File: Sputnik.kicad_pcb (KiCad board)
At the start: 4 copper layers, 130 x 60 mm, 78 parts, among them IC1 EP4CE10F17, J1 Pinheader_2x5_TH_WALL, U1 SN74LVC2T45, U10 SN74LVC8T245, U11 SN74LVC8T245, U12 SN74LVC8T245, U13 SN74LVC8T245, U14 SN74LVC8T245, U15 SN74LVC8T245, U16 SN74LVC2T45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

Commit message: Up
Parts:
- C16, U4: moved to B.Cu
- moved C16 51.4 mm to (231.4, 61.5), turned to 180 degrees
- moved U4 14.8 mm to (210.0, 61.5)
- moved U3 1.03 mm to (231.2, 61.5), turned to 270 degrees
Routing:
- net /Zorro/~SLAVEn: track 10.6 -> 15.7 mm
- net GND: track 126.6 -> 129.1 mm, vias 41 -> 43
- net +3V3: track 30.7 -> 33.1 mm, vias 7 -> 9

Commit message: More routing
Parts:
- C14, C34: moved to B.Cu
- moved C34 70.7 mm to (197.2, 65.0), turned to 180 degrees
- moved R8 1.50 mm to (197.2, 63.5)
- moved C14 1.30 mm to (197.2, 58.0), turned to 180 degrees
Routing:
- net /FPGA/TDO: track 0.71 -> 59.9 mm
- net /FPGA/TCK: track 0.71 -> 52.6 mm
- net /Zorro/~BRn: track 0.00 -> 47.3 mm, vias 0 -> 1
- net /Zorro/~CFGOUTn: track 0.00 -> 34.5 mm, vias 0 -> 2
- net /Zorro/~MTACK: track 0.00 -> 30.3 mm
- net /Zorro/~CINH: track 0.00 -> 25.8 mm, vias 0 -> 1
- net GND: track 129.1 -> 136.7 mm, vias 43 -> 50
- net Net-(R8-Pad1): track 0.00 -> 4.45 mm
- net +3V3: track 33.1 -> 34.6 mm, vias 9 -> 10
- net +5VDC: track 23.5 -> 24.9 mm, vias 8 -> 9

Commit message: And more
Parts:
- moved C42 2.83 mm to (152.7, 64.3), turned to 90 degrees
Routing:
- net Net-(R8-Pad1): track 4.45 -> 65.5 mm
- net /Zorro/~DTACK: track 0.00 -> 18.7 mm
- net GND: track 136.7 -> 153.9 mm, vias 50 -> 64
- net /Zorro/E_CLOCK: track 4.72 -> 20.6 mm, vias 1 -> 2
- net /Zorro/~INT6: track 0.00 -> 15.5 mm
- net /Zorro/~INT2: track 0.00 -> 13.7 mm, vias 0 -> 1
- net /Zorro/AD12: track 3.30 -> 12.5 mm
- net /Zorro/~CINH: track 25.8 -> 32.0 mm
- net +5VDC: track 24.9 -> 28.3 mm, vias 9 -> 13
- net +3V3: track 34.6 -> 36.3 mm, vias 10 -> 13
- net /Zorro/AD29: track 11.1 -> 11.8 mm
- net /Zorro/~DS0: track 24.9 -> 25.5 mm

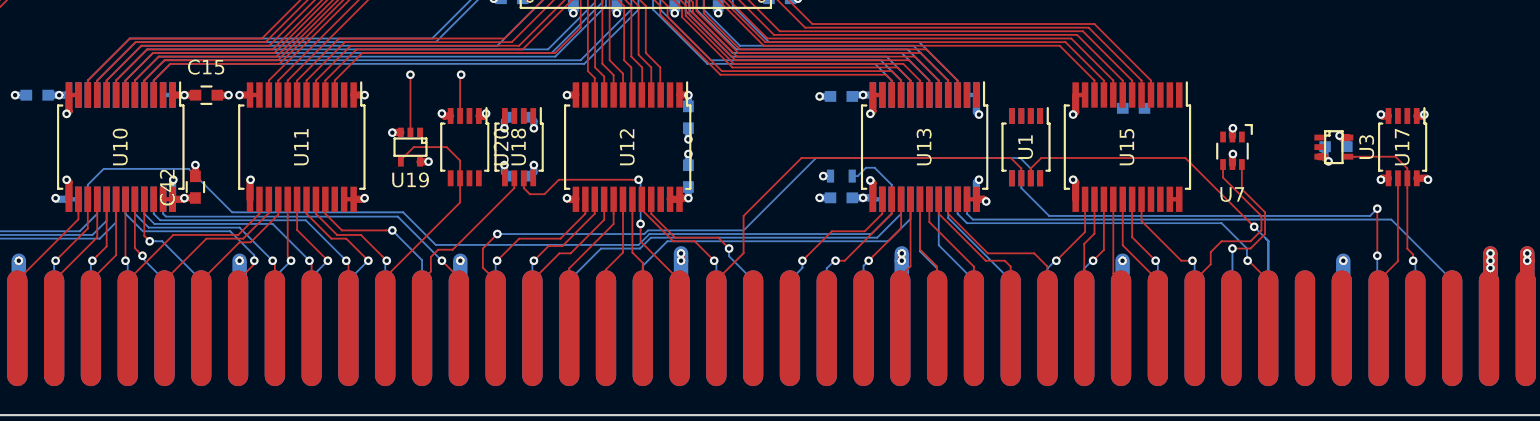
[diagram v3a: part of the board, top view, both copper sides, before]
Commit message: More routing and caps
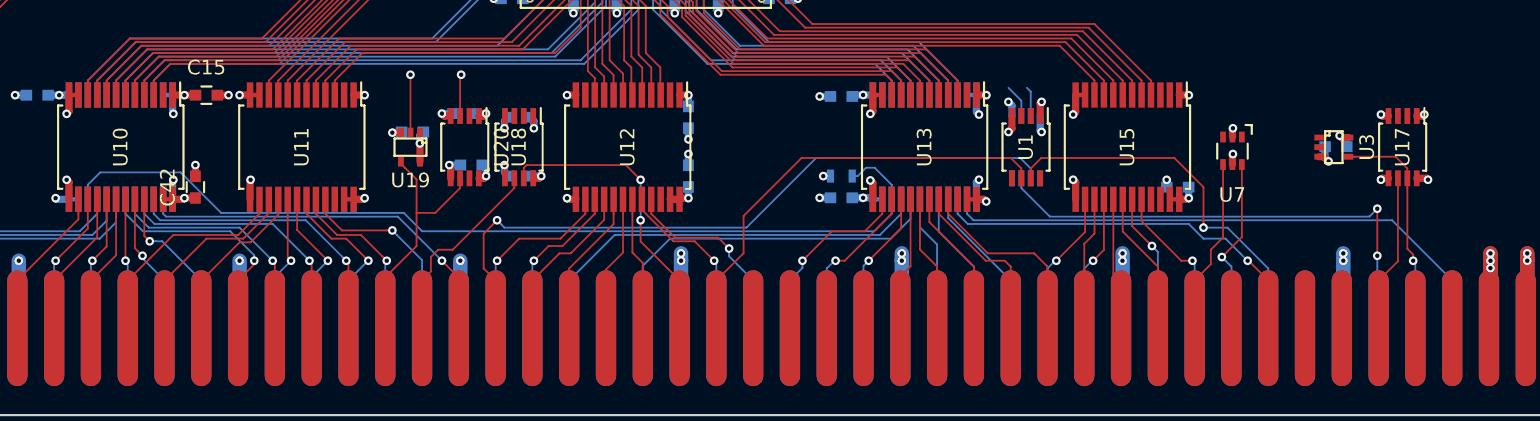
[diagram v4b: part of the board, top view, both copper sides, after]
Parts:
- added C61: 0,1, Capacitors_SMD:C_0603, B.Cu at (171.7, 62.7)
- added C62: 0,1, Capacitors_SMD:C_0603, B.Cu at (171.2, 59.2)
- added C63: 0,1, Capacitors_SMD:C_0603, B.Cu at (167.6, 60.5)
- moved C43 6.23 mm to (220.5, 64.3), turned to 180 degrees
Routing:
- net GND: track 153.9 -> 162.2 mm, vias 64 -> 71
- net +3V3: track 36.3 -> 42.1 mm, vias 13 -> 17
- net /Zorro/~CINH: track 32.0 -> 26.3 mm
- net /Zorro/~INT6: track 15.5 -> 12.1 mm
- net +5VDC: track 28.3 -> 30.8 mm, vias 13 -> 14
- net /FPGA/nCFGOUTn: track 0.00 -> 2.31 mm
- net /FPGA/nBR: track 0.00 -> 2.06 mm
- net /Zorro/~INT2: track 13.7 -> 12.1 mm
- net /Zorro/~DTACK: track 18.7 -> 17.3 mm
- net Net-(R8-Pad1): track 65.5 -> 64.5 mm
- net /Zorro/~BRn: track 47.3 -> 48.2 mm
- net (no net): vias 0 -> 1

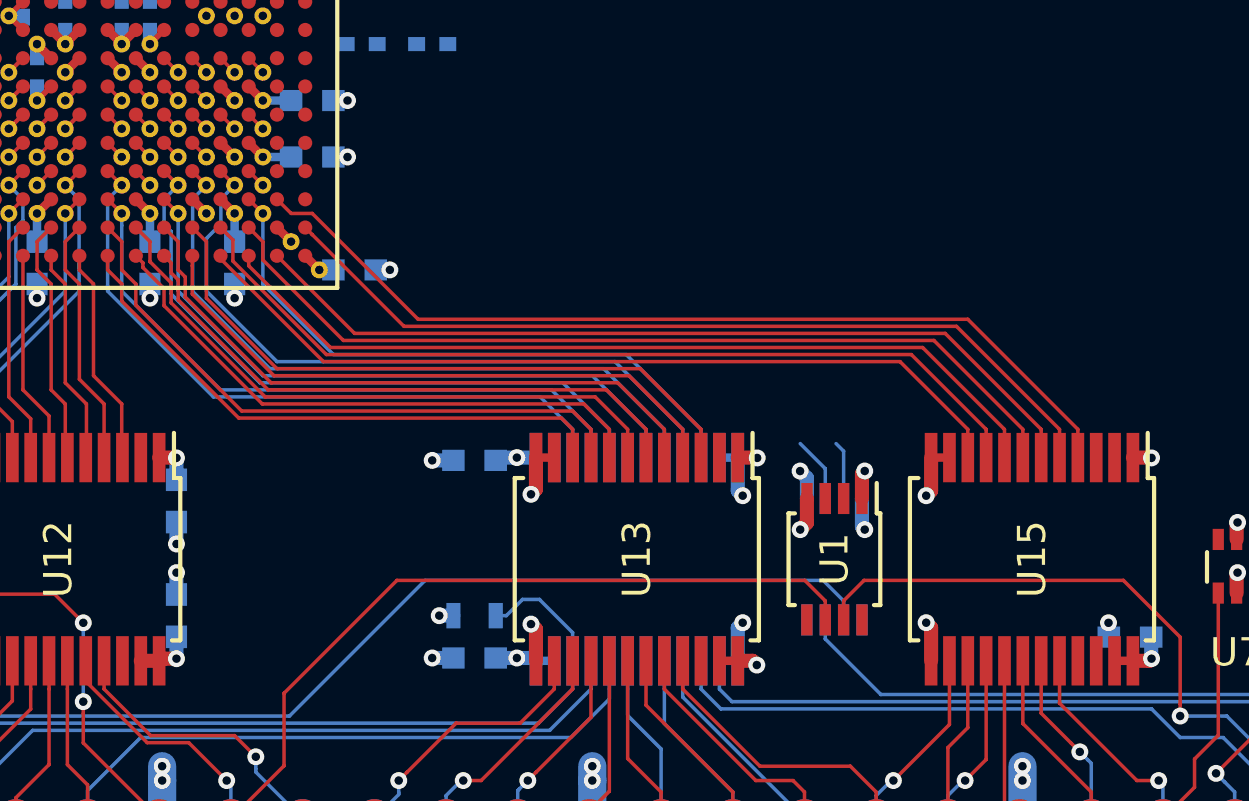
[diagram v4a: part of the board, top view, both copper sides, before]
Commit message: Added nMTACK and nCINH signals
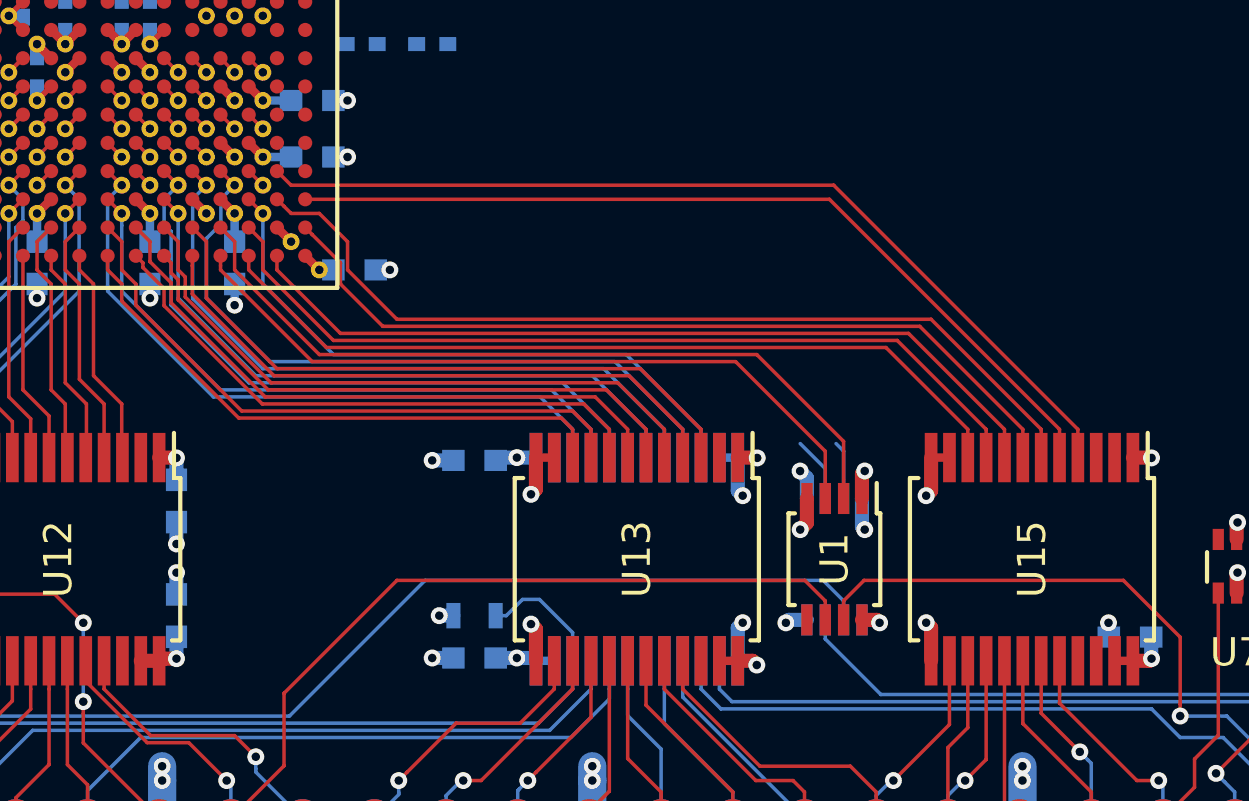
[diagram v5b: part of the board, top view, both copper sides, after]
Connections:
- IC1 pad N15: Net-(IC1-PadN15) -> /FPGA/A_5
- IC1 pad P15: /FPGA/A_5 -> /FPGA/A_4
- IC1 pad P16: Net-(IC1-PadP16) -> /FPGA/A_6
- IC1 pad R13: /FPGA/A_7 -> /FPGA/nCINH
- IC1 pad R14: /FPGA/A_3 -> /FPGA/A_7
- IC1 pad R16: /FPGA/A_6 -> /FPGA/A_3
- IC1 pad T13: /FPGA/nLOCK -> /FPGA/nMTACK
- IC1 pad T14: /FPGA/A_2 -> /FPGA/nLOCK
- IC1 pad T15: /FPGA/A_4 -> /FPGA/A_2
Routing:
- net /FPGA/nCINH: track 0.00 -> 27.8 mm
- net /FPGA/nMTACK: track 0.00 -> 26.4 mm
- net /FPGA/A_3: track 31.8 -> 29.8 mm
- net +5VDC: track 30.8 -> 32.2 mm, vias 14 -> 16
- net /FPGA/A_4: track 30.6 -> 32.0 mm
- net /FPGA/A_2: track 30.5 -> 29.6 mm
- net /FPGA/A_7: track 31.5 -> 30.7 mm
- net /FPGA/nLOCK: track 30.1 -> 29.3 mm

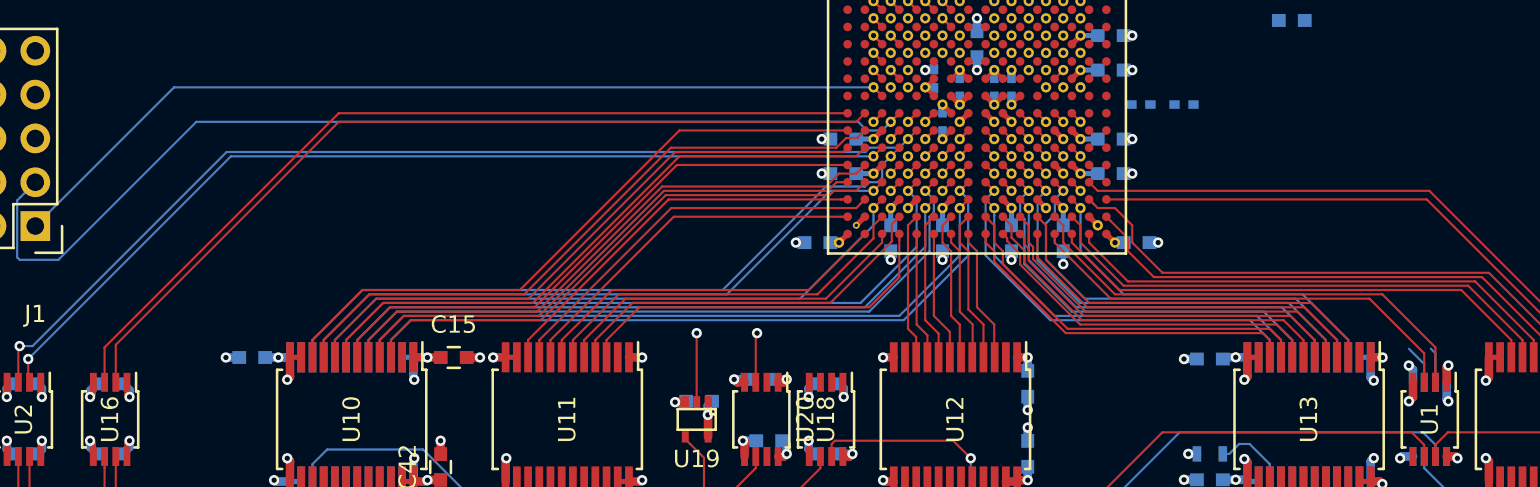
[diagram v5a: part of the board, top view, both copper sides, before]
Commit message: Squeezed nBG and E_CLOCK as well
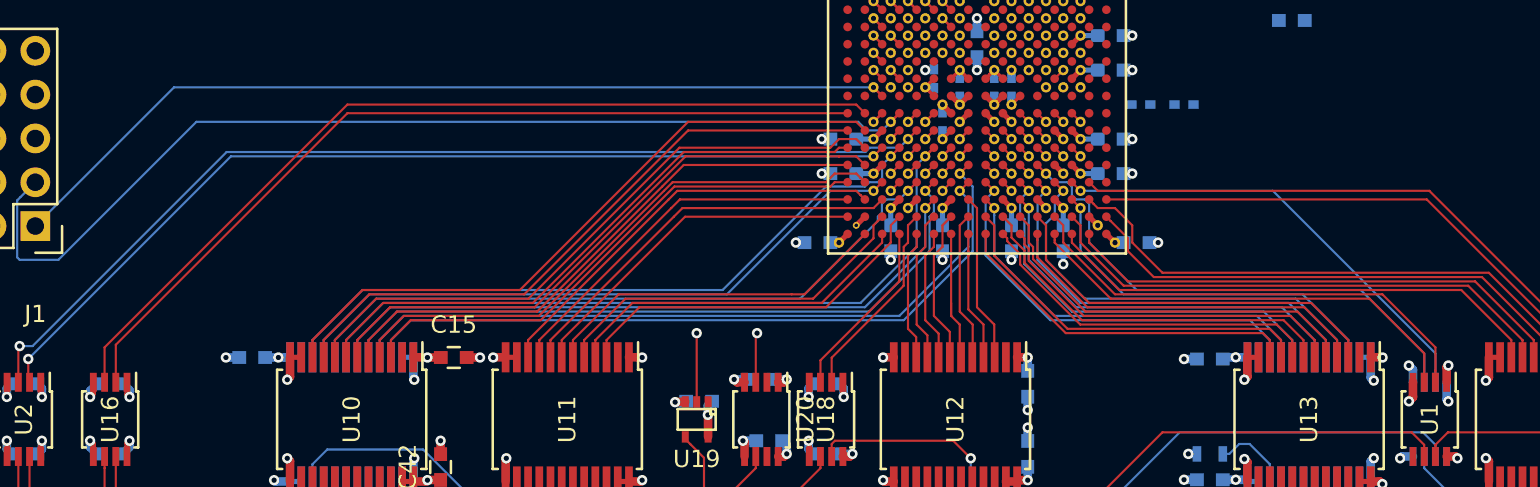
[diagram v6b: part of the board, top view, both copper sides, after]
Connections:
- IC1 pad J1: /FPGA/7M_ -> /FPGA/SenseZ3
- IC1 pad J2: /FPGA/SenseZ3 -> /FPGA/7M_
- IC1 pad K1: /FPGA/SD_5 -> /FPGA/SD_4
- IC1 pad K2: /FPGA/SD_4 -> /FPGA/SD_5
- IC1 pad L1: /FPGA/SD_6 -> /FPGA/SD_3
- IC1 pad L2: /FPGA/SD_3 -> /FPGA/SD_6
- IC1 pad L6: Net-(IC1-PadL6) -> /FPGA/nCCS
- IC1 pad M1: /FPGA/SD_7 -> /FPGA/SD_2
- IC1 pad M12: Net-(IC1-PadM12) -> /FPGA/nCFGOUTn
- IC1 pad M2: /FPGA/SD_2 -> /FPGA/SD_7
- IC1 pad M8: Net-(IC1-PadM8) -> /FPGA/nBGACK
- IC1 pad N1: /FPGA/SD_1 -> /FPGA/SD_0
- IC1 pad N14: Net-(IC1-PadN14) -> /FPGA/nBR
- IC1 pad N2: /FPGA/SD_0 -> /FPGA/SD_1
- IC1 pad N5: /FPGA/nCCS -> /FPGA/DOE_
- IC1 pad N8: /FPGA/nBGACK -> /FPGA/READ_
- IC1 pad P1: /FPGA/AD_24 -> /FPGA/AD_25
- IC1 pad P2: /FPGA/AD_25 -> /FPGA/AD_24
- IC1 pad P3: /FPGA/DOE_ -> /FPGA/AD_26
- IC1 pad P8: /FPGA/READ_ -> /FPGA/AD_16
- IC1 pad R1: /FPGA/AD_26 -> /FPGA/AD_27
- IC1 pad R3: /FPGA/AD_28 -> /FPGA/AD_29
- IC1 pad R4: /FPGA/AD_30 -> /FPGA/AD_31
- IC1 pad R5: /FPGA/AD_23 -> /FPGA/E_CLOCK_
- IC1 pad R6: /FPGA/AD_21 -> /FPGA/AD_22
- IC1 pad R7: /FPGA/AD_19 -> /FPGA/AD_20
- IC1 pad R8: /FPGA/AD_17 -> /FPGA/AD_18
- IC1 pad T2: /FPGA/AD_27 -> /FPGA/AD_28
- IC1 pad T3: /FPGA/AD_29 -> /FPGA/AD_30
- IC1 pad T4: /FPGA/AD_31 -> /FPGA/nBG
- IC1 pad T5: /FPGA/AD_22 -> /FPGA/AD_23
- IC1 pad T6: /FPGA/AD_20 -> /FPGA/AD_21
- IC1 pad T7: /FPGA/AD_18 -> /FPGA/AD_19
- IC1 pad T8: /FPGA/AD_16 -> /FPGA/AD_17
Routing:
- net /FPGA/nCFGOUTn: track 2.31 -> 30.5 mm
- net /FPGA/nBR: track 2.06 -> 26.9 mm
- net /FPGA/E_CLOCK_: track 0.00 -> 11.6 mm
- net /FPGA/nBG: track 0.00 -> 10.5 mm
- net /FPGA/AD_26: track 21.2 -> 23.6 mm
- net /FPGA/DOE_: track 36.7 -> 39.0 mm
- net /FPGA/AD_16: track 7.78 -> 9.78 mm
- net /FPGA/nCCS: track 40.5 -> 42.5 mm
- net /FPGA/AD_28: track 22.3 -> 20.5 mm
- net /FPGA/AD_30: track 22.2 -> 20.5 mm
- net /FPGA/SD_1: track 31.9 -> 33.3 mm
- net /FPGA/SD_5: track 37.1 -> 38.5 mm
- net /FPGA/AD_22: track 7.41 -> 8.82 mm
- net /FPGA/7M_: track 50.7 -> 52.1 mm
- net /FPGA/SD_7: track 33.6 -> 35.0 mm
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
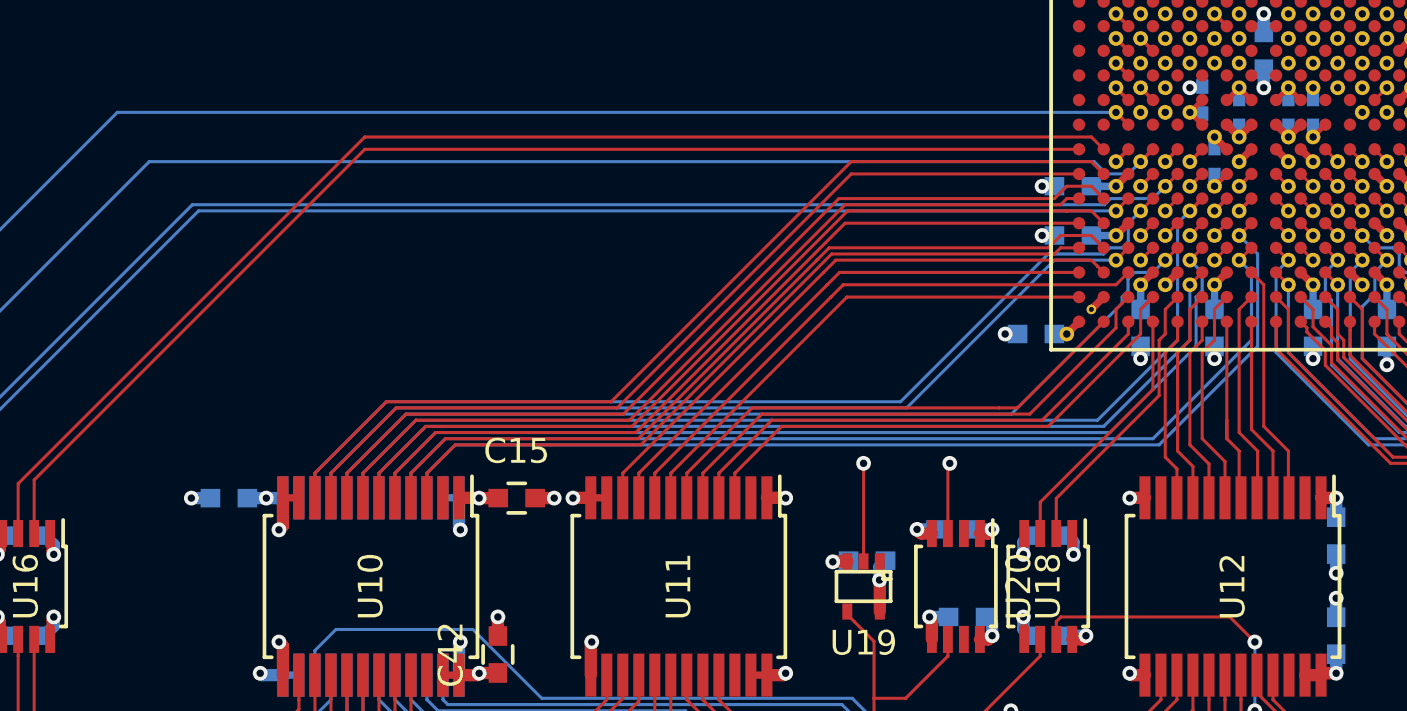
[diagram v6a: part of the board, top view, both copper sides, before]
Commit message: nDTACK* rerouted
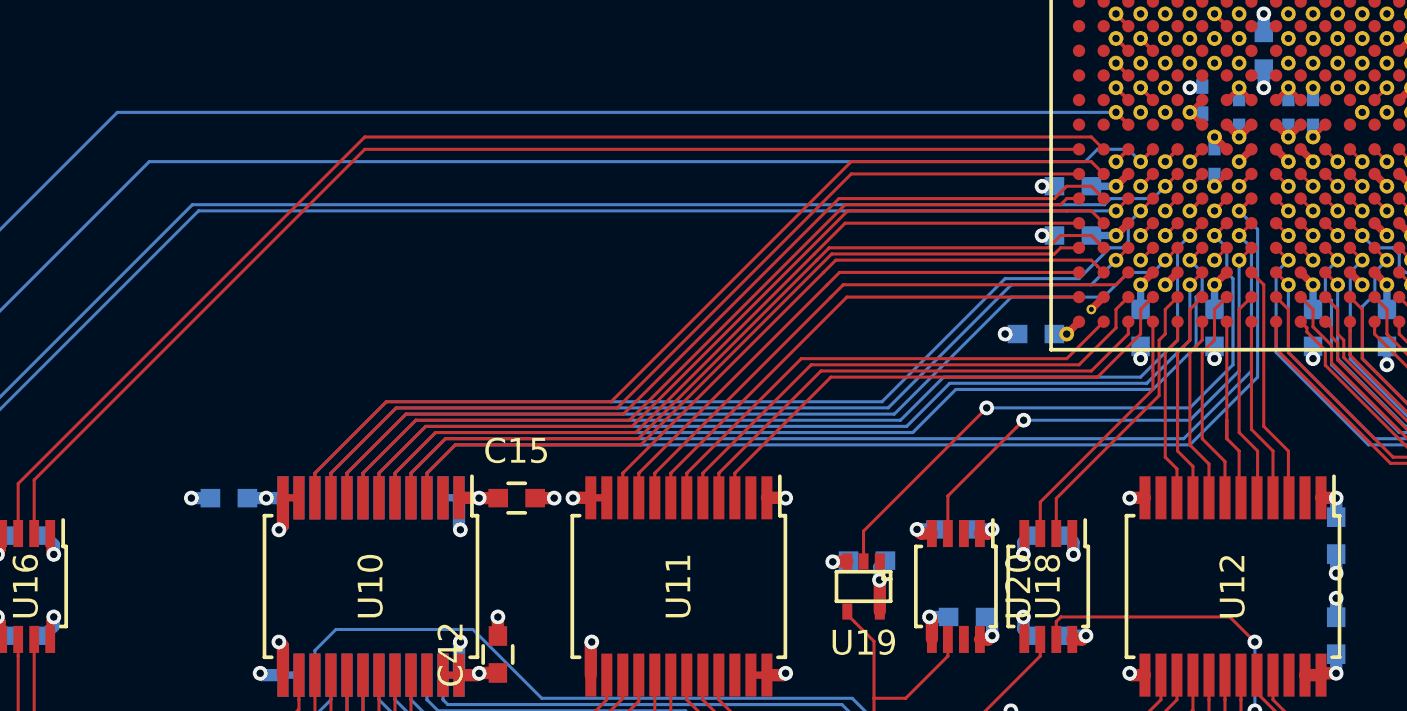
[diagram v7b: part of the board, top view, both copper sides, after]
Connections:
- IC1 pad L6: /FPGA/nCCS -> Net-(IC1-PadL6)
- IC1 pad L8: Net-(IC1-PadL8) -> /FPGA/nBGACK
- IC1 pad M6: /FPGA/nDTACK_OUT -> /FPGA/nCCS
- IC1 pad M7: /FPGA/nDTACK -> /FPGA/nDTACK_OUT
- IC1 pad M8: /FPGA/nBGACK -> /FPGA/READ_
- IC1 pad N8: /FPGA/READ_ -> /FPGA/nDTACK
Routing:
- net /FPGA/nDTACK_OUT: track 21.8 -> 25.3 mm
- net /FPGA/nBGACK: track 42.4 -> 44.1 mm
- net /FPGA/READ_: track 41.5 -> 43.3 mm
- net /FPGA/nCCS: track 42.5 -> 41.5 mm
- net /FPGA/nDTACK: track 19.7 -> 20.7 mm
- net Net-(IC1-PadL6): track 0.00 -> 0.71 mm
- net Net-(IC1-PadL8): track 0.71 -> 0.00 mm

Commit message: Up
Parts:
- moved R1 53.0 mm to (208.0, 62.0), turned to 270 degrees
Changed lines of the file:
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@@
   )
   (module Resistors_SMD:R_0603 (layer F.Cu)
-    (at 251.580953 31.864999)
+    (at 208 62 270)
     (descr "Resistor SMD 0603, reflow soldering, Vishay (see dcrcw.pdf)")
     (tags "resistor 0603")
     (attr smd)
-    (fp_text reference R1 (at 0 -1.9) (layer F.SilkS)
+    (fp_text reference R1 (at 0 -1.9 270) (layer F.SilkS)
       (effects (font (size 1 1) (thickness 0.15)))
     )
-    (fp_text value TBD (at 0 1.9) (layer F.Fab)
+    (fp_text value TBD (at 0 1.9 270) (layer F.Fab)
       (effects (font (size 1 1) (thickness 0.15)))
     )
@@
     (fp_line (start 0.5 0.675) (end -0.5 0.675) (layer F.SilkS) (width 0.15))
     (fp_line (start -0.5 -0.675) (end 0.5 -0.675) (layer F.SilkS) (width 0.15))
-    (pad 1 smd rect (at -0.75 0) (size 0.5 0.9) (layers F.Cu F.Paste F.Mask)
+    (pad 1 smd rect (at -0.75 0 270) (size 0.5 0.9) (layers F.Cu F.Paste F.Mask)
       (net 163 +3V3))
-    (pad 2 smd rect (at 0.75 0) (size 0.5 0.9) (layers F.Cu F.Paste F.Mask)
+    (pad 2 smd rect (at 0.75 0 270) (size 0.5 0.9) (layers F.Cu F.Paste F.Mask)
       (net 250 /Zorro/nBUSMASTER))
     (model Resistors_SMD.3dshapes/R_0603.wrl
